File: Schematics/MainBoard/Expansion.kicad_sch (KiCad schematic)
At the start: 8 parts, among them J9 DIN41612_02x32_AC

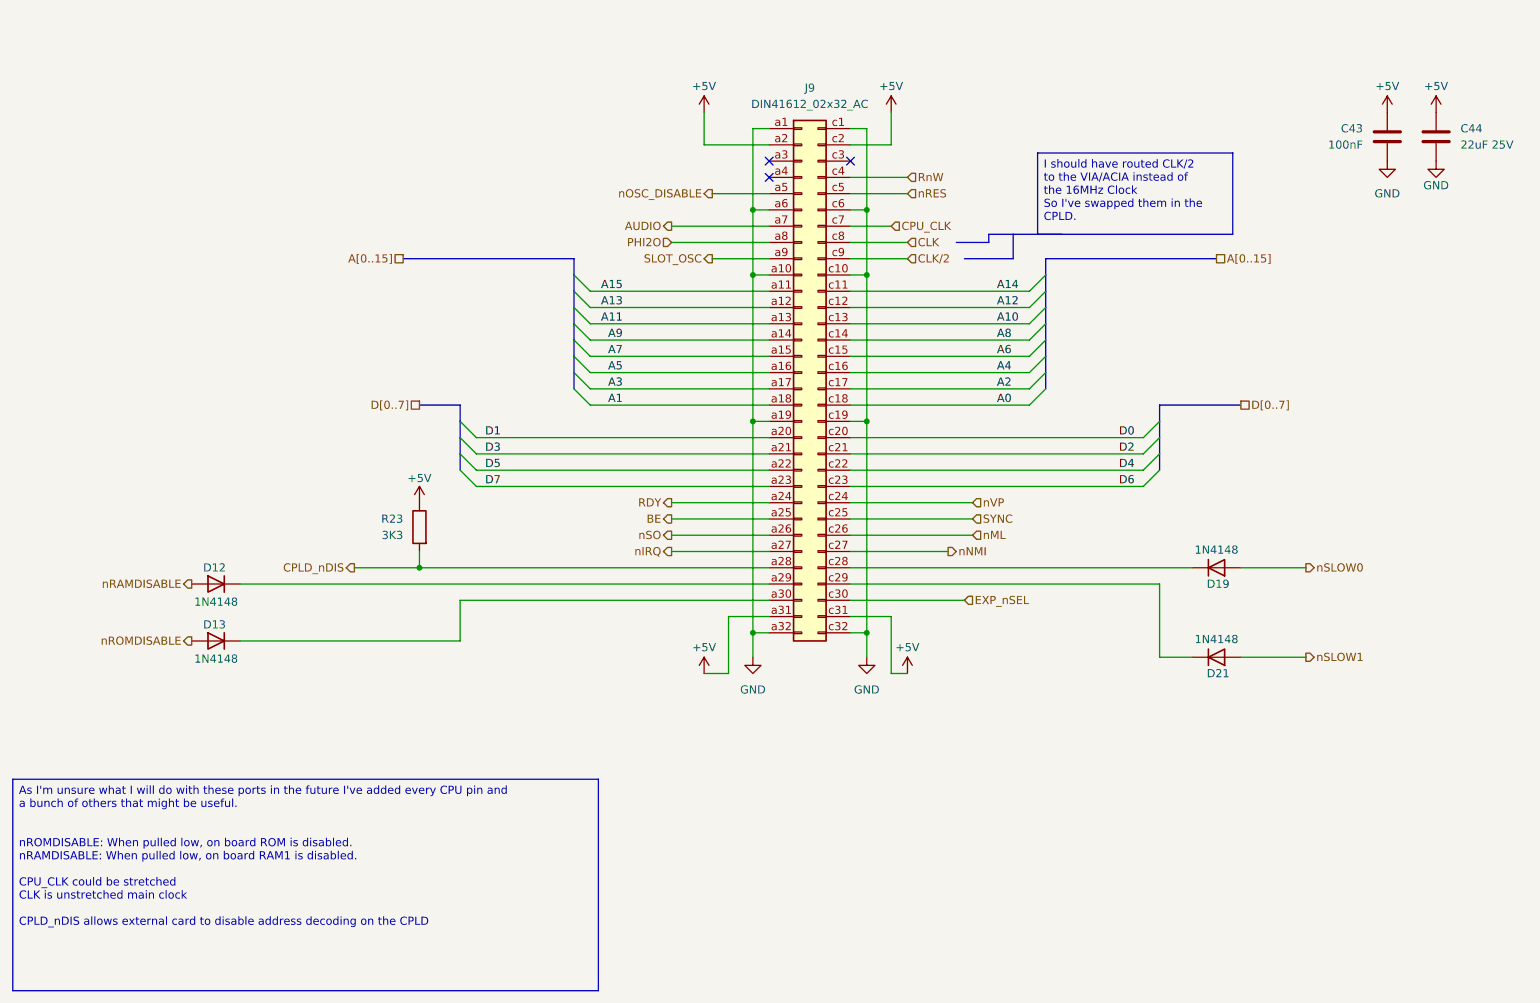
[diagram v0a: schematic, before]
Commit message: Move to a single board for everything (keyboard and main board)
Aim is to save height
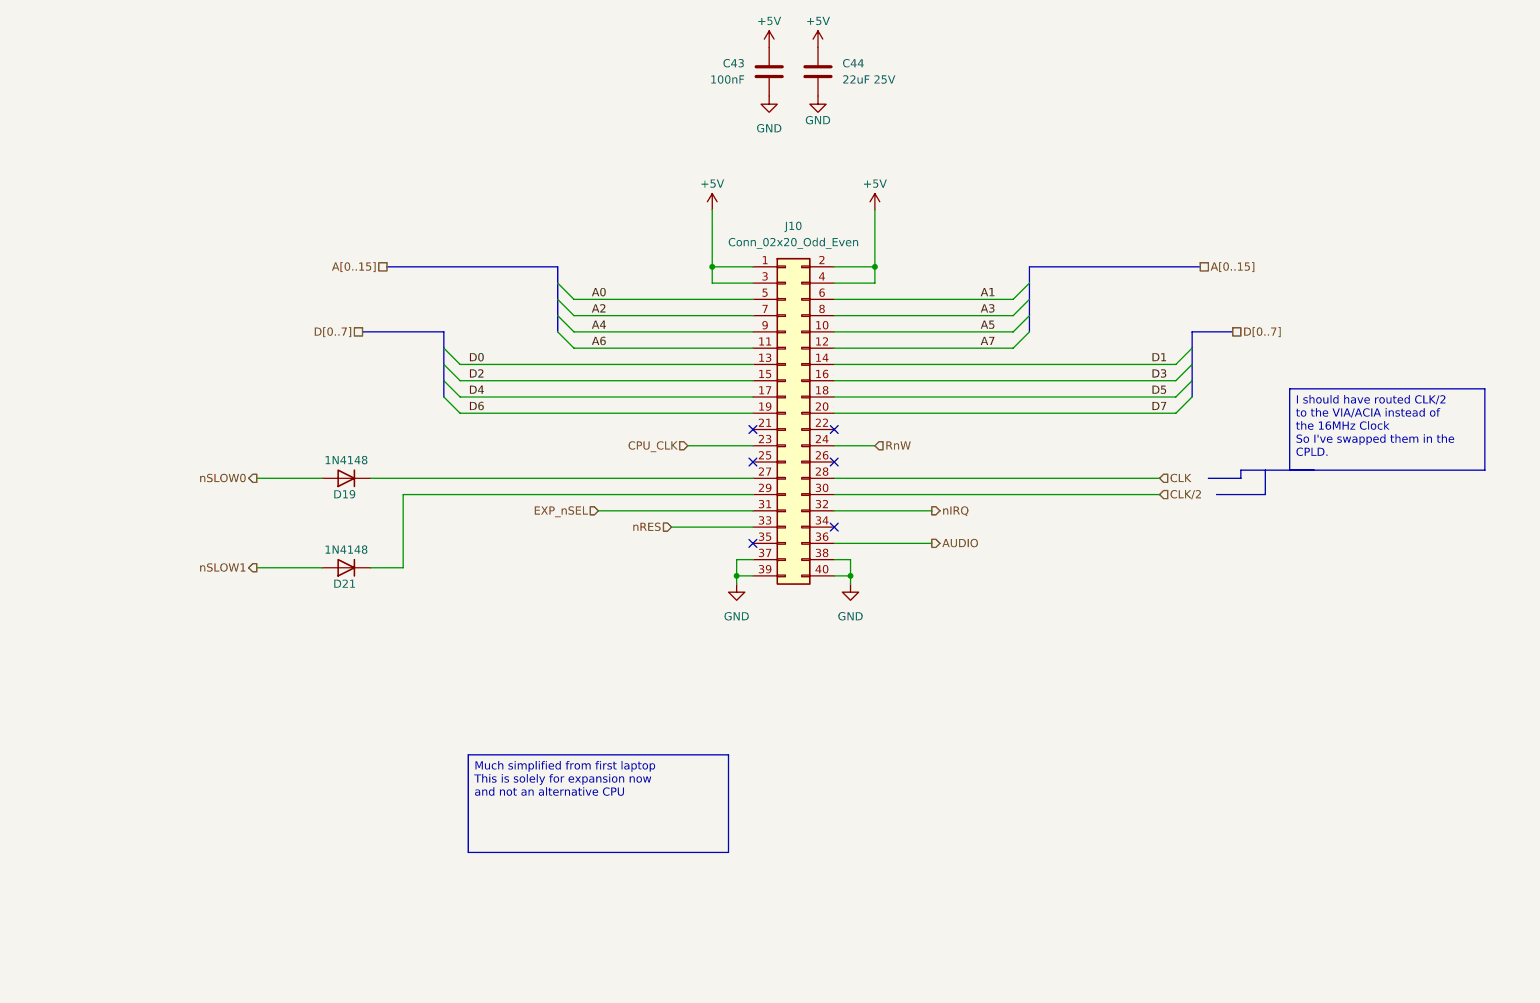
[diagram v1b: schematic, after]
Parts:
- removed D12, D13: 1N4148, Diode_THT:D_DO-35_SOD27_P7.62mm_Horizontal, symbol Diode:1N4148
- removed J9: DIN41612_02x32_AC, Connector_DIN:DIN41612_R_2x32_Female_Horizontal_THT, symbol Connector:DIN41612_02x32_AC
- removed R23: 3K3, Resistor_SMD:R_0402_1005Metric, symbol Device:R
- added J10: Conn_02x20_Odd_Even, symbol Connector_Generic:Conn_02x20_Odd_Even
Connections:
- net +5V: now also J10.1 (Pin_1), J10.2 (Pin_2), J10.3 (Pin_3), J10.4 (Pin_4)
- net A0: now also J10.5 (Pin_5)
- net A1: now also J10.6 (Pin_6)
- net A2: now also J10.7 (Pin_7)
- net A3: now also J10.8 (Pin_8)
- net A4: now also J10.9 (Pin_9)
- net A5: now also J10.10 (Pin_10)
- net A6: now also J10.11 (Pin_11)
- net A7: now also J10.12 (Pin_12)
- net AUDIO: now also J10.36 (Pin_36)
- net CLK: now also J10.28 (Pin_28)
- net CLK/2: now also J10.30 (Pin_30)
- net CPU_CLK: now also J10.23 (Pin_23)
- net D0: now also J10.13 (Pin_13)
- net D1: now also J10.14 (Pin_14)
- net D2: now also J10.15 (Pin_15)
- net D3: now also J10.16 (Pin_16)
- net D4: now also J10.17 (Pin_17)
- net D5: now also J10.18 (Pin_18)
- net D6: now also J10.19 (Pin_19)
- net D7: now also J10.20 (Pin_20)
- net EXP_nSEL: now also J10.31 (Pin_31)
- net GND: now also J10.37 (Pin_37), J10.38 (Pin_38), J10.39 (Pin_39), J10.40 (Pin_40)
- net RnW: now also J10.24 (Pin_24)
- net nIRQ: now also J10.32 (Pin_32)
- net nRES: now also J10.33 (Pin_33)
- net at D21.1 (K): now also J10.29 (Pin_29)
- net at D19.1 (K): now also J10.27 (Pin_27)
- no-connect marks 3 -> 6
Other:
- moved on the sheet: C43, C44, D19, D21

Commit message: rough placement of parts to help with 3D CAD
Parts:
- J10: footprint (none) -> Connector_PinHeader_2.54mm:PinHeader_2x20_P2.54mm_Horizontal
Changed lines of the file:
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@@
 			)
 		)
-		(property "Footprint" ""
+		(property "Footprint" "Connector_PinHeader_2.54mm:PinHeader_2x20_P2.54mm_Horizontal"
 			(at 151.13 100.33 0)
 			(effects

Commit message: Work on PCB
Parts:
- C43: footprint Capacitor_SMD:C_0603_1608Metric -> Capacitor_SMD:C_0402_1005Metric
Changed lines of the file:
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@@
 			)
 		)
-		(property "Footprint" "Capacitor_SMD:C_0603_1608Metric"
+		(property "Footprint" "Capacitor_SMD:C_0402_1005Metric"
 			(at 147.6248 50.8 0)
 			(effects
